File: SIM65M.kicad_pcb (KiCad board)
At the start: 4 copper layers, 40 x 40 mm, 21 parts, among them J3 Conn_01x10_Pin, Q1 AO3400A, Q2 DTC143ZUAT106, Q3 DTC143ZUAT106, U1 SIM65M_C7495025, U2 BWGNSCNX25-25W4, U4 TXS0102DCUR, U5 XC6206P282MR-G

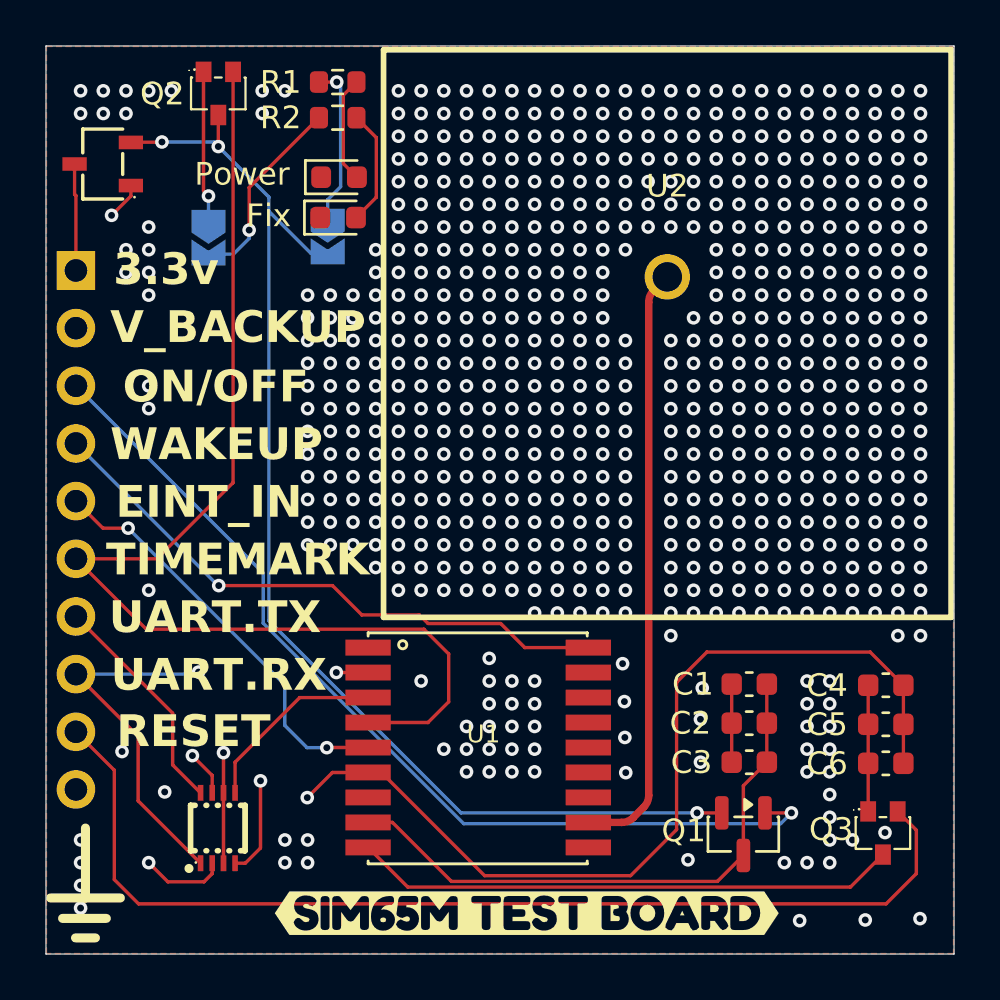
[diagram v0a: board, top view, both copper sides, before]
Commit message: agregado UFL
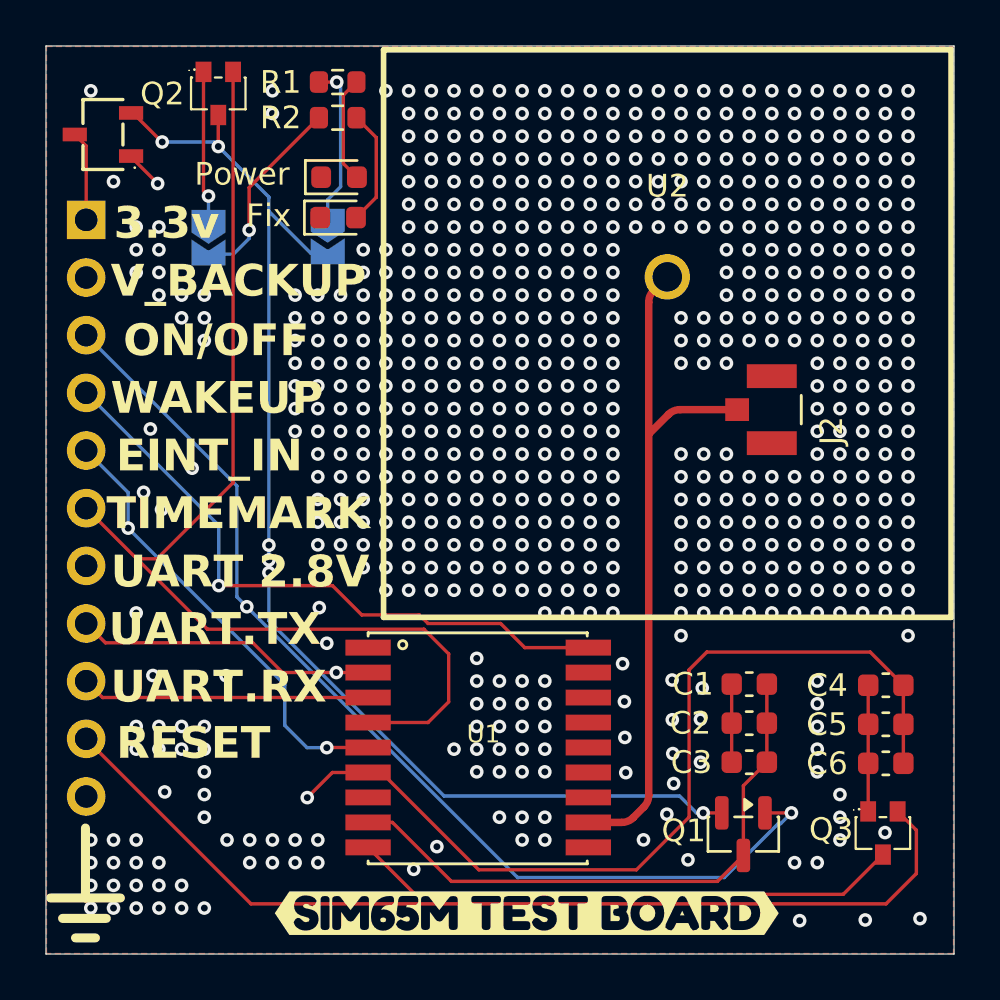
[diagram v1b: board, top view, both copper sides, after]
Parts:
- removed J3: Conn_01x10_Pin, Connector_PinHeader_2.54mm:PinHeader_1x10_P2.54mm_Vertical
- removed U4: TXS0102DCUR, EasyEDA:VSON8_L2.0-W2.3-P0.50-LS3.1-BL
- added J1: Conn_01x11_Pin, Connector_PinHeader_2.54mm:PinHeader_1x11_P2.54mm_Vertical, B.Cu at (193.1, 82.5)
- added J2: U.FL-R-SMT_10_, Snapeda:U.FL-R-SMT_10_-foot, F.Cu at (223.3, 90.9)
- moved U5 1.30 mm to (193.8, 78.8)
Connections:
- U1 pad 2: /SHIFTER.RX -> /SIM65M.TX
- U1 pad 3: /SHIFTER.TX -> /SIM65M.RX
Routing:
- net /PIN.3.3v: track 30.4 -> 3.97 mm, vias 1 -> 0
- net /2.8V: track 87.0 -> 64.1 mm, vias 4 -> 6
- net /SHIFTER.RX: track 12.2 -> 0.00 mm, vias 2 -> 0
- net /SIM65M.TX: track 10.0 -> 19.8 mm, vias 0 -> 1
- net /SHIFTER.TX: track 8.39 -> 0.00 mm
- net /RF_IN: track 26.4 -> 30.8 mm
- net /ON/OFF: track 42.2 -> 46.2 mm, vias 1 -> 2
- net /PIN.RESET: track 47.1 -> 43.2 mm
- net GND: track 14.5 -> 10.7 mm, vias 681 -> 671
- net /PIN.V_BACKUP: track 67.7 -> 71.4 mm
- net /SIM65M.RX: track 16.1 -> 12.7 mm, vias 1 -> 0
- net /SIM65M.timemark: track 50.6 -> 48.4 mm
- net /SIM65M.wakeUP: track 26.3 -> 28.4 mm
- net /SIM65M.EINT_IN: track 18.4 -> 19.8 mm
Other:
- board text added: "UART 2.8V"

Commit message: rediseño etapa RF, agregada bifurcacion para activa/pasiva, mejoras generales en RF
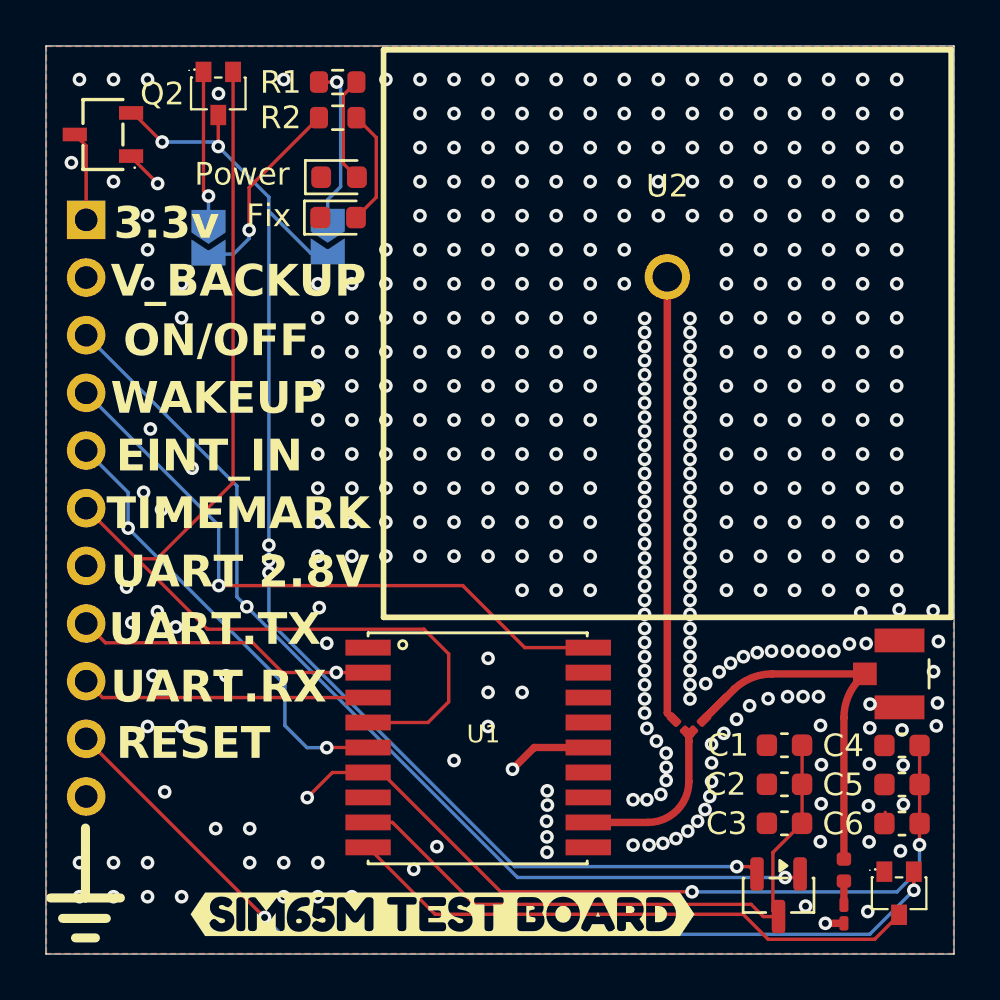
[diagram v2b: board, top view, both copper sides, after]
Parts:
- added L1: 22uH, Inductor_SMD:L_0402_1005Metric, F.Cu at (226.5, 111.2)
- added R3: 0, Resistor_SMD:R_0201_0603Metric_Pad0.64x0.40mm_HandSolder, F.Cu at (219.3, 104.8)
- added R4: 0, Resistor_SMD:R_0201_0603Metric_Pad0.64x0.40mm_HandSolder, F.Cu at (220.0, 104.8)
- added R5: 22, Resistor_SMD:R_0201_0603Metric_Pad0.64x0.40mm_HandSolder, F.Cu at (226.5, 113.1)
- moved J2 12.9 mm to (228.9, 102.5)
- moved kibuzzard-6A279BE5 3.71 mm to (208.8, 113.1)
- moved C1 3.11 mm to (223.9, 105.7)
- moved C2 3.11 mm to (223.9, 107.4)
- moved C3 3.11 mm to (223.9, 109.1)
- moved Q1 3.11 mm to (223.6, 112.3)
- moved C4 2.75 mm to (229.0, 105.7)
- moved C5 2.75 mm to (229.0, 107.4)
- moved C6 2.75 mm to (229.0, 109.1)
- moved Q3 2.75 mm to (228.9, 112.2)
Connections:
- J2 pad SIG: /RF_IN -> /RF_IN_2
- U1 pad 11: /RF_IN -> /RF_IN_1
- U1 pad 14: unconnected-(U1-VDD_ANT-Pad14) -> /RF_IN_4
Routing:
- net /RF_IN_4: track 0.00 -> 24.1 mm, vias 0 -> 2
- net /RF_IN_2: track 0.00 -> 17.6 mm
- net /RF_IN: track 30.8 -> 20.3 mm
- net GND: track 10.7 -> 1.70 mm, vias 671 -> 407
- net /RF_IN_1: track 0.00 -> 7.45 mm
- net /SIM65M.TX: track 19.8 -> 13.4 mm
- net /PIN.V_BACKUP: track 71.4 -> 66.5 mm, vias 1 -> 3
- net /2.8V: track 64.1 -> 66.8 mm
- net /SIM65M.VCC: track 26.1 -> 28.0 mm
- net /ON/OFF: track 46.2 -> 44.3 mm
- net /PIN.RESET: track 43.2 -> 41.7 mm, vias 0 -> 2
- net /SIM65M.RESET_N: track 24.3 -> 25.5 mm
- net /RF_IN_3: track 0.00 -> 1.05 mm
